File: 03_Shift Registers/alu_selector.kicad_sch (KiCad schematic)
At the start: 1 part, among them U7 74LS245

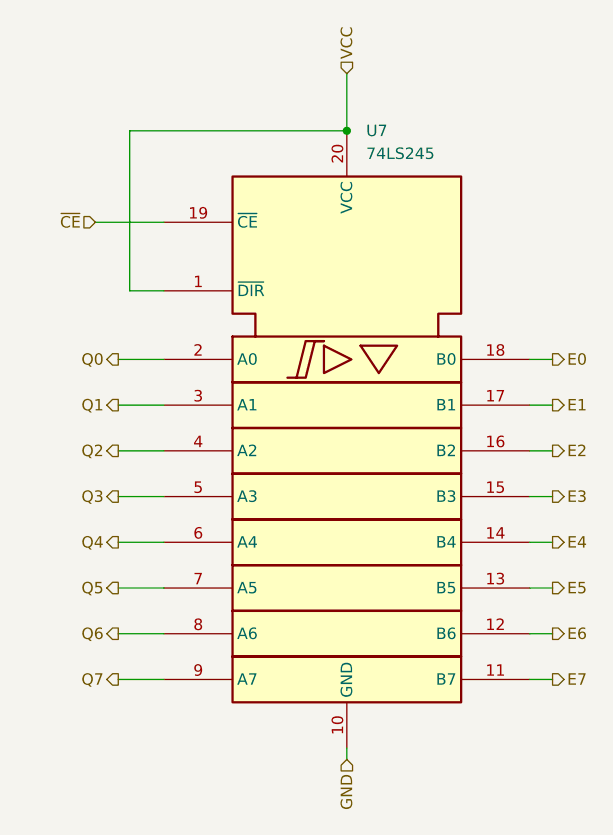
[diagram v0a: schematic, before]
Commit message: Last revision of the cpu, all boards have been ordered. Implementation to be tested and documented in following commits.
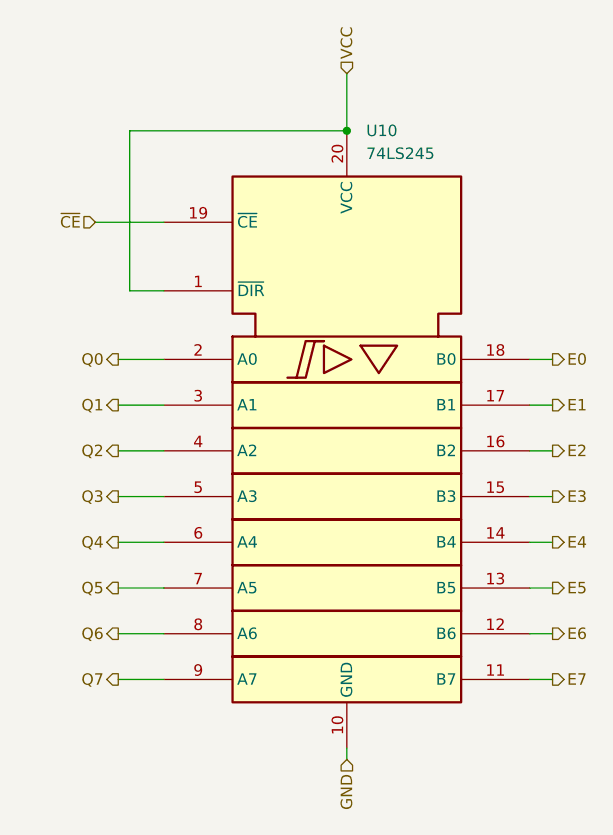
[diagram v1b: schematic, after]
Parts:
- renumbered U7 to U10
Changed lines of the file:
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@@
 		(dnp no)
 		(fields_autoplaced yes)
-		(property "Reference" "U7"
+		(property "Reference" "U10"
 			(at 157.0833 66.04 0)
 			(effects
@@
 			(project "Shift Registers"
 				(path "/0bbead8f-a697-49a3-a523-e82b541d79df/1c81a464-d6d3-4091-8abc-25dbb97686e9"
-					(reference "U9")
+					(reference "U12")
 					(unit 1)
 				)
 				(path "/0bbead8f-a697-49a3-a523-e82b541d79df/7d4e5ddf-de15-484d-b168-7ee485d2ef5c"
-					(reference "U7")
+					(reference "U10")
 					(unit 1)
 				)
 				(path "/0bbead8f-a697-49a3-a523-e82b541d79df/ad9c6a51-1a08-48a4-bf98-de20c0b3ace8"
-					(reference "U10")
+					(reference "U13")
 					(unit 1)
 				)
 				(path "/0bbead8f-a697-49a3-a523-e82b541d79df/c991ae6d-c124-4703-812b-feaebbda5d76"
-					(reference "U8")
+					(reference "U11")
 					(unit 1)
 				)
